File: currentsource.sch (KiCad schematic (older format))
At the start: 18 parts, among them Q3 FQD17P06TM, Q4 2N7000, U1 THAT320, U2 THAT320, U3 LM358

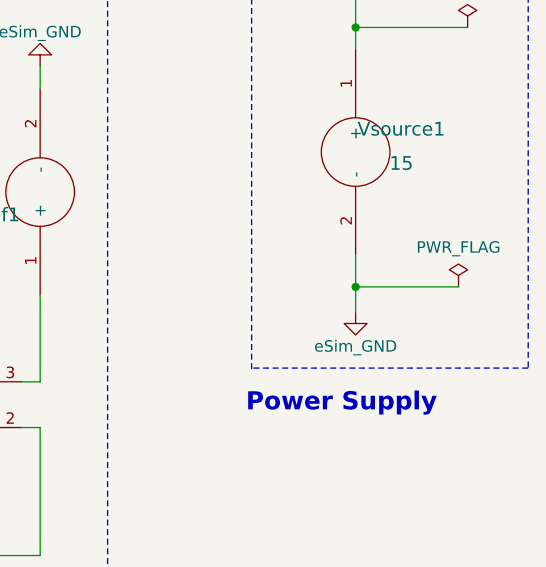
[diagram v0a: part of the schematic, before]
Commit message: removed ground powerflag.
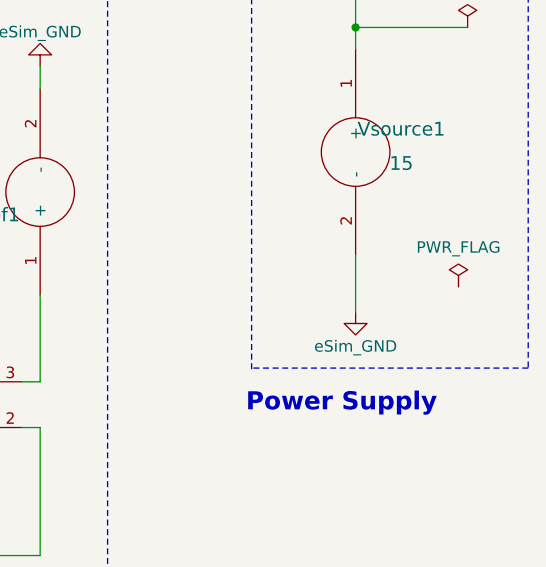
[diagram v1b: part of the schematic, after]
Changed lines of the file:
@@
 Power Supply
 Wire Wire Line
-	9515 2840 9515 2980
-Wire Wire Line
-	9965 2980 9515 2980
-Connection ~ 9515 2980
-Wire Wire Line
-	9515 2980 9515 3090
+	9515 2840 9515 3090
 $EndSCHEMATC

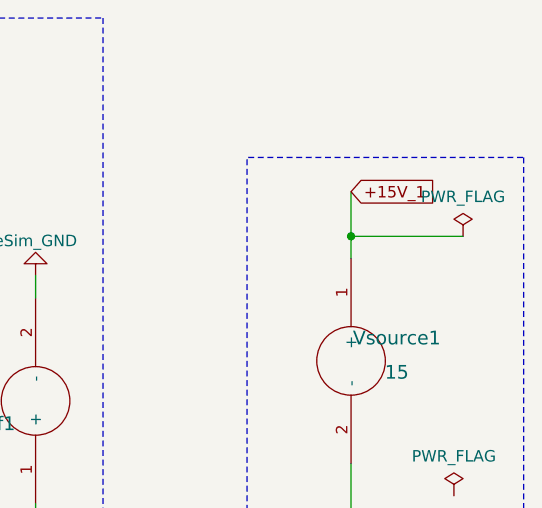
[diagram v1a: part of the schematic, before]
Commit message: removed ground and +15V_1 powerflag.
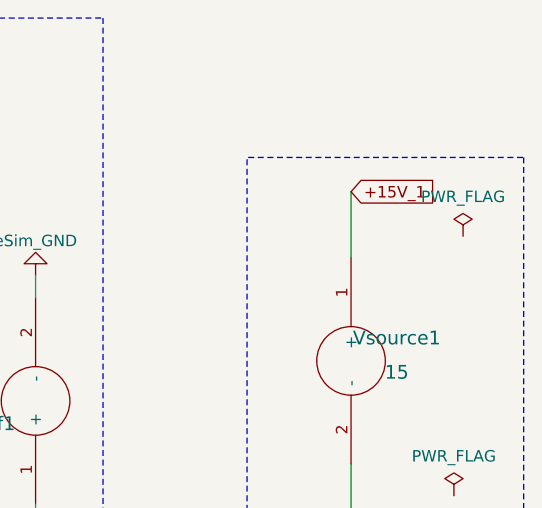
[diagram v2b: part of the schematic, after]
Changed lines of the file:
@@
 Text GLabel 7755 3895 3    50   Input ~ 0
 +15V_1
-Wire Wire Line
-	9515 1650 9515 1845
 $Comp
 L power:PWR_FLAG #FLG0101
@@
 	1    0    0    -1
 $EndComp
-Wire Wire Line
-	10005 1845 9515 1845
-Connection ~ 9515 1845
-Wire Wire Line
-	9515 1845 9515 1940
 Wire Wire Line
 	4085 6070 4350 6070
@@
 Wire Wire Line
 	9515 2840 9515 3090
+Wire Wire Line
+	9515 1650 9515 1940
 $EndSCHEMATC
